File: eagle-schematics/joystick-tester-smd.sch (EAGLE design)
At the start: 12 parts

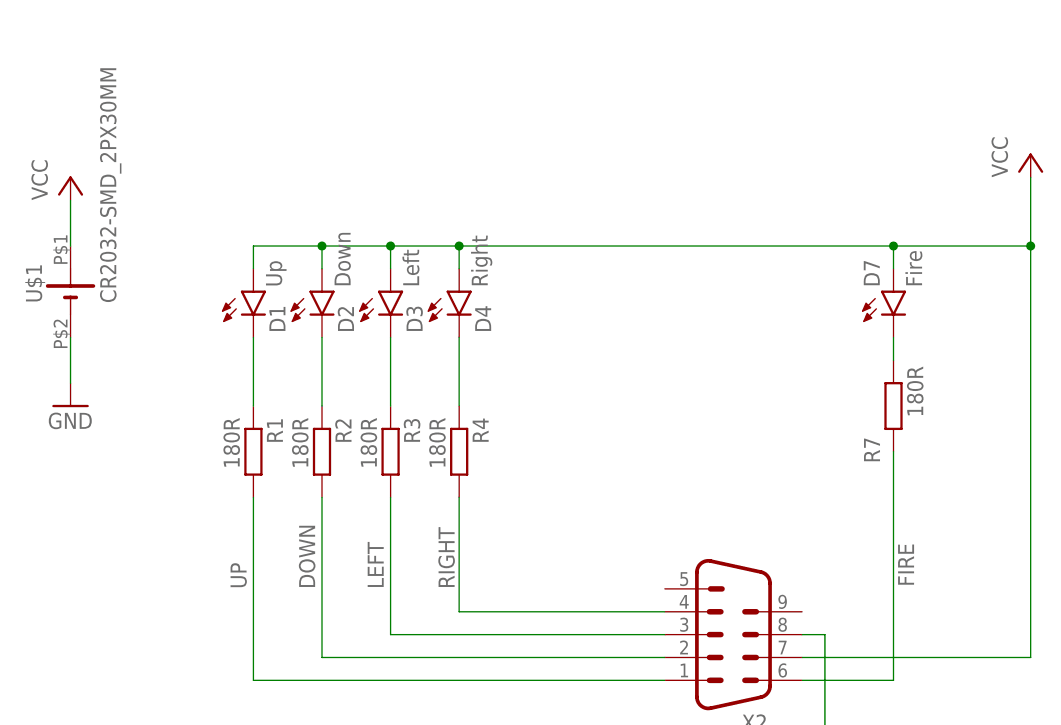
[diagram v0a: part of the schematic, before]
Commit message: Updated battery layout
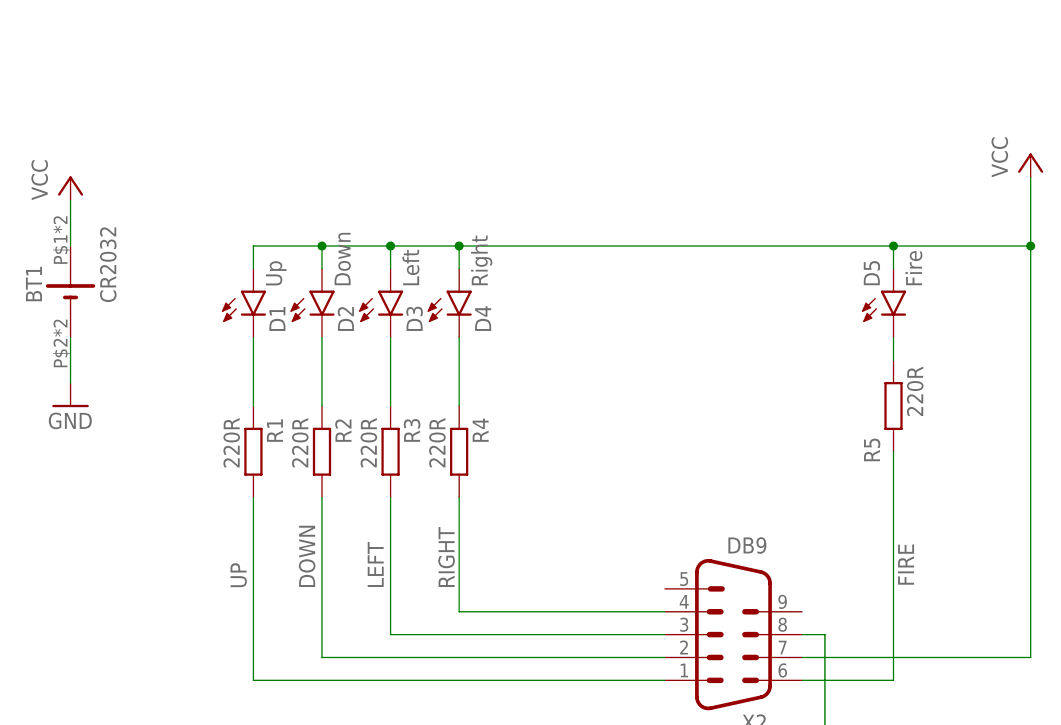
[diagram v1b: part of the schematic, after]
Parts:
- removed U$1: CR2032-SMD_2PX30MM, Per:CR2032-SMD_2PX30MM
- added BT1: CR2032, Per:CR2032-COMBO-20MM-30MM_SMD
- R1, R2, R3, R4, R5: value 180R -> 220R
- X2: value (none) -> DB9
- renumbered D7 to D5, R7 to R5
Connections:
- net GND: now also BT1.-; no longer U$1.-
- net VCC: now also BT1.+; no longer U$1.+

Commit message: Update schematics
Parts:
- added U$1: RETRONINJA_TEXT, PCBGraphics:RETRONINJA_TEXT
- renumbered X2 to X1
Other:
- note added: "2"
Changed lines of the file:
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@@
 <grid distance="0.1" unitdist="inch" unit="inch" style="lines" multiple="1" display="no" altdistance="0.01" altunitdist="inch" altunit="inch"/>
 <layers>
-<layer number="1" name="Top" color="4" fill="1" visible="yes" active="no"/>
-<layer number="16" name="Bottom" color="1" fill="1" visible="yes" active="no"/>
-<layer number="17" name="Pads" color="2" fill="1" visible="yes" active="no"/>
-<layer number="18" name="Vias" color="2" fill="1" visible="yes" active="no"/>
-<layer number="19" name="Unrouted" color="6" fill="1" visible="yes" active="no"/>
-<layer number="20" name="Dimension" color="24" fill="1" visible="yes" active="no"/>
-<layer number="21" name="tPlace" color="7" fill="1" visible="yes" active="no"/>
-<layer number="22" name="bPlace" color="7" fill="1" visible="yes" active="no"/>
-<layer number="23" name="tOrigins" color="15" fill="1" visible="yes" active="no"/>
-<layer number="24" name="bOrigins" color="15" fill="1" visible="yes" active="no"/>
-<layer number="25" name="tNames" color="7" fill="1" visible="yes" active="no"/>
-<layer number="26" name="bNames" color="7" fill="1" visible="yes" active="no"/>
-<layer number="27" name="tValues" color="7" fill="1" visible="yes" active="no"/>
-<layer number="28" name="bValues" color="7" fill="1" visible="yes" active="no"/>
+<layer number="1" name="Top" color="4" fill="1" visible="no" active="no"/>
+<layer number="16" name="Bottom" color="1" fill="1" visible="no" active="no"/>
+<layer number="17" name="Pads" color="2" fill="1" visible="no" active="no"/>
+<layer number="18" name="Vias" color="2" fill="1" visible="no" active="no"/>
+<layer number="19" name="Unrouted" color="6" fill="1" visible="no" active="no"/>
+<layer number="20" name="Dimension" color="24" fill="1" visible="no" active="no"/>
+<layer number="21" name="tPlace" color="7" fill="1" visible="no" active="no"/>
+<layer number="22" name="bPlace" color="7" fill="1" visible="no" active="no"/>
+<layer number="23" name="tOrigins" color="15" fill="1" visible="no" active="no"/>
+<layer number="24" name="bOrigins" color="15" fill="1" visible="no" active="no"/>
+<layer number="25" name="tNames" color="7" fill="1" visible="no" active="no"/>
+<layer number="26" name="bNames" color="7" fill="1" visible="no" active="no"/>
+<layer number="27" name="tValues" color="7" fill="1" visible="no" active="no"/>
+<layer number="28" name="bValues" color="7" fill="1" visible="no" active="no"/>
 <layer number="29" name="tStop" color="7" fill="3" visible="no" active="no"/>
 <layer number="30" name="bStop" color="7" fill="6" visible="no" active="no"/>
@@
 <layer number="35" name="tGlue" color="7" fill="4" visible="no" active="no"/>
 <layer number="36" name="bGlue" color="7" fill="5" visible="no" active="no"/>
-<layer number="37" name="tTest" color="7" fill="1" visible="yes" active="no"/>
-<layer number="38" name="bTest" color="7" fill="1" visible="yes" active="no"/>
+<layer number="37" name="tTest" color="7" fill="1" visible="no" active="no"/>
+<layer number="38" name="bTest" color="7" fill="1" visible="no" active="no"/>
 <layer number="39" name="tKeepout" color="4" fill="11" visible="no" active="no"/>
 <layer number="40" name="bKeepout" color="1" fill="11" visible="no" active="no"/>
@@
 <layer number="44" name="Drills" color="7" fill="1" visible="no" active="no"/>
 <layer number="45" name="Holes" color="7" fill="1" visible="no" active="no"/>
-<layer number="46" name="Milling" color="3" fill="1" visible="yes" active="no"/>
-<layer number="47" name="Measures" color="7" fill="1" visible="yes" active="no"/>
-<layer number="48" name="Document" color="7" fill="1" visible="yes" active="no"/>
-<layer number="49" name="Reference" color="7" fill="1" visible="yes" active="no"/>
-<layer number="50" name="dxf" color="7" fill="1" visible="yes" active="no"/>
-<layer number="51" name="tDocu" color="7" fill="1" visible="yes" active="no"/>
-<layer number="52" name="bDocu" color="7" fill="1" visible="yes" active="no"/>
-<layer number="53" name="tPadExt" color="7" fill="1" visible="yes" active="no"/>
-<layer number="54" name="bPadExt" color="1" fill="1" visible="yes" active="no"/>
-<layer number="56" name="wert" color="7" fill="1" visible="yes" active="no"/>
-<layer number="57" name="tCAD" color="7" fill="1" visible="yes" active="no"/>
-<layer number="59" name="tCarbon" color="7" fill="1" visible="yes" active="no"/>
-<layer number="60" name="bCarbon" color="7" fill="1" visible="yes" active="no"/>
+<layer number="46" name="Milling" color="3" fill="1" visible="no" active="no"/>
+<layer number="47" name="Measures" color="7" fill="1" visible="no" active="no"/>
+<layer number="48" name="Document" color="7" fill="1" visible="no" active="no"/>
+<layer number="49" name="Reference" color="7" fill="1" visible="no" active="no"/>
+<layer number="50" name="dxf" color="7" fill="1" visible="no" active="no"/>
+<layer number="51" name="tDocu" color="7" fill="1" visible="no" active="no"/>
+<layer number="52" name="bDocu" color="7" fill="1" visible="no" active="no"/>
+<layer number="53" name="tPadExt" color="7" fill="1" visible="no" active="no"/>
+<layer number="54" name="bPadExt" color="1" fill="1" visible="no" active="no"/>
+<layer number="56" name="wert" color="7" fill="1" visible="no" active="no"/>
+<layer number="57" name="tCAD" color="7" fill="1" visible="no" active="no"/>
+<layer number="59" name="tCarbon" color="7" fill="1" visible="no" active="no"/>
+<layer number="60" name="bCarbon" color="7" fill="1" visible="no" active="no"/>
 <layer number="88" name="SimResults" color="9" fill="1" visible="yes" active="yes"/>
 <layer number="89" name="SimProbes" color="9" fill="1" visible="yes" active="yes"/>
@@
 </layers>
 <schematic xreflabel="%F%N/%S.%C%R" xrefpart="/%S.%C%R">
+<description>Tester for 9-pin Atari and Commodore compatible joysticks</description>
 <attributes>
+<attribute name="REV" value="2"/>
 </attributes>
 <variantdefs>
@@
 <part name="P+3" library="supply1" library_urn="urn:adsk.eagle:library:371" deviceset="VCC" device=""/>
 <part name="GND2" library="supply1" library_urn="urn:adsk.eagle:library:371" deviceset="GND" device=""/>
-<part name="X2" library="con-subd" library_urn="urn:adsk.eagle:library:189" deviceset="M09" device="D" package3d_urn="urn:adsk.eagle:package:10300/1" value="DB9"/>
+<part name="X1" library="con-subd" library_urn="urn:adsk.eagle:library:189" deviceset="M09" device="D" package3d_urn="urn:adsk.eagle:package:10300/1" value="DB9"/>
 <part name="BT1" library="Per" deviceset="CR2032" device="-COMBO-20MM-30MM_SMD" value="CR2032"/>
+<part name="FRAME1" library="frames" library_urn="urn:adsk.eagle:library:229" deviceset="DINA4_L" device=""/>
+<part name="U$1" library="PCBGraphics" deviceset="RETRONINJA_TEXT" device=""/>
 </parts>
 <sheets>
 <sheet>
+<description>Tester for 9-pin Atari and Commodore compatible joysticks</description>
 <plain>
+<text x="121.92" y="-45.72" size="2.54" layer="94">2</text>
 </plain>
 <instances>
@@
 <attribute name="VALUE" x="-66.04" y="43.18" size="1.778" layer="96"/>
 </instance>
-<instance part="X2" gate="-1" x="10.16" y="20.32" smashed="yes" rot="R180">
+<instance part="X1" gate="-1" x="10.16" y="20.32" smashed="yes" rot="R180">
 <attribute name="VALUE" x="13.97" y="31.115" size="1.778" layer="96" rot="R180"/>
 <attribute name="NAME" x="13.97" y="11.43" size="1.778" layer="95" rot="R180"/>
@@
 <attribute name="VALUE" x="-58.42" y="57.15" size="1.778" layer="96" rot="R90"/>
 </instance>
+<instance part="FRAME1" gate="G$1" x="-132.08" y="-53.34" smashed="yes"/>
+<instance part="FRAME1" gate="G$2" x="30.48" y="-53.34" smashed="yes">
+<attribute name="LAST_DATE_TIME" x="43.18" y="-52.07" size="2.54" layer="94"/>
+<attribute name="SHEET" x="116.84" y="-52.07" size="2.54" layer="94"/>
+<attribute name="DRAWING_NAME" x="48.26" y="-34.29" size="2.54" layer="94"/>
+</instance>
+<instance part="U$1" gate="G$1" x="119.38" y="-7.62" smashed="yes"/>
 </instances>
 <busses>
@@
 <wire x1="-43.18" y1="15.24" x2="-43.18" y2="35.56" width="0.1524" layer="91"/>
 <label x="-43.942" y="25.4" size="1.778" layer="95" rot="R90"/>
-<pinref part="X2" gate="-1" pin="1"/>
+<pinref part="X1" gate="-1" pin="1"/>
 </segment>
 </net>
@@
 <wire x1="-35.56" y1="17.78" x2="-35.56" y2="35.56" width="0.1524" layer="91"/>
 <label x="-36.322" y="25.4" size="1.778" layer="95" rot="R90"/>
-<pinref part="X2" gate="-1" pin="2"/>
+<pinref part="X1" gate="-1" pin="2"/>
 </segment>
 </net>
@@
 <wire x1="-27.94" y1="20.32" x2="-27.94" y2="35.56" width="0.1524" layer="91"/>
 <label x="-28.702" y="25.4" size="1.778" layer="95" rot="R90"/>
-<pinref part="X2" gate="-1" pin="3"/>
+<pinref part="X1" gate="-1" pin="3"/>
 </segment>
 </net>
@@
 <wire x1="-20.32" y1="22.86" x2="-20.32" y2="35.56" width="0.1524" layer="91"/>
 <label x="-20.828" y="25.4" size="1.778" layer="95" rot="R90"/>
-<pinref part="X2" gate="-1" pin="4"/>
+<pinref part="X1" gate="-1" pin="4"/>
 </segment>
 </net>
@@
 <pinref part="GND1" gate="1" pin="GND"/>
 <wire x1="20.32" y1="20.32" x2="20.32" y2="7.62" width="0.1524" layer="91"/>
-<pinref part="X2" gate="-1" pin="8"/>
+<pinref part="X1" gate="-1" pin="8"/>
 <wire x1="20.32" y1="20.32" x2="17.78" y2="20.32" width="0.1524" layer="91"/>
 </segment>
@@
 <wire x1="27.94" y1="15.24" x2="27.94" y2="40.64" width="0.1524" layer="91"/>
 <label x="30.226" y="25.654" size="1.778" layer="95" rot="R90"/>
-<pinref part="X2" gate="-1" pin="6"/>
+<pinref part="X1" gate="-1" pin="6"/>
 <wire x1="27.94" y1="15.24" x2="17.78" y2="15.24" width="0.1524" layer="91"/>
 </segment>
@@
 <wire x1="-20.32" y1="60.96" x2="-20.32" y2="63.5" width="0.1524" layer="91"/>
 <junction x="-20.32" y="63.5"/>
-<pinref part="X2" gate="-1" pin="7"/>
+<pinref part="X1" gate="-1" pin="7"/>
 <wire x1="43.18" y1="17.78" x2="17.78" y2="17.78" width="0.1524" layer="91"/>
 <pinref part="D5" gate="G$1" pin="A"/>

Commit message: Update schematics
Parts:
- removed U$1: RETRONINJA_TEXT, PCBGraphics:RETRONINJA_TEXT
- X1: value DB9 -> DE-9M
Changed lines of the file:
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@@
 <part name="P+3" library="supply1" library_urn="urn:adsk.eagle:library:371" deviceset="VCC" device=""/>
 <part name="GND2" library="supply1" library_urn="urn:adsk.eagle:library:371" deviceset="GND" device=""/>
-<part name="X1" library="con-subd" library_urn="urn:adsk.eagle:library:189" deviceset="M09" device="D" package3d_urn="urn:adsk.eagle:package:10300/1" value="DB9"/>
+<part name="X1" library="con-subd" library_urn="urn:adsk.eagle:library:189" deviceset="M09" device="D" package3d_urn="urn:adsk.eagle:package:10300/1" value="DE-9M"/>
 <part name="BT1" library="Per" deviceset="CR2032" device="-COMBO-20MM-30MM_SMD" value="CR2032"/>
 <part name="FRAME1" library="frames" library_urn="urn:adsk.eagle:library:229" deviceset="DINA4_L" device=""/>
-<part name="U$1" library="PCBGraphics" deviceset="RETRONINJA_TEXT" device=""/>
+<part name="U$1" library="PCBGraphics" deviceset="RETRONINJA_TEXT_SCH-ONLY" device=""/>
 </parts>
 <sheets>
